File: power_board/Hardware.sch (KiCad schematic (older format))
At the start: 87 parts, among them J1 Conn_01x02, J10 Conn_01x04, J11 Conn_01x04, J12 Conn_02x13_Odd_Even, J13 Conn_01x02, J14 Conn_01x02, J2 Conn_01x04, J3 Conn_01x02, J4 Conn_01x02_Male, J5 Conn_01x02_Male, J6 Conn_01x02_Male, J7 Conn_01x02_Male, J8 Conn_01x03, J9 Conn_01x03, Q1 BD140, Q10 BC548, Q11 BD139, Q12 BD139, Q2 BD140, Q3 BC548, Q4 BC548, Q5 BD139, Q6 BD139, Q7 BD140, Q8 BD140, Q9 BC548, U1 LM393, U2 TCRT5000, U3 LM324, U4 HC-05, U5 TCRT5000

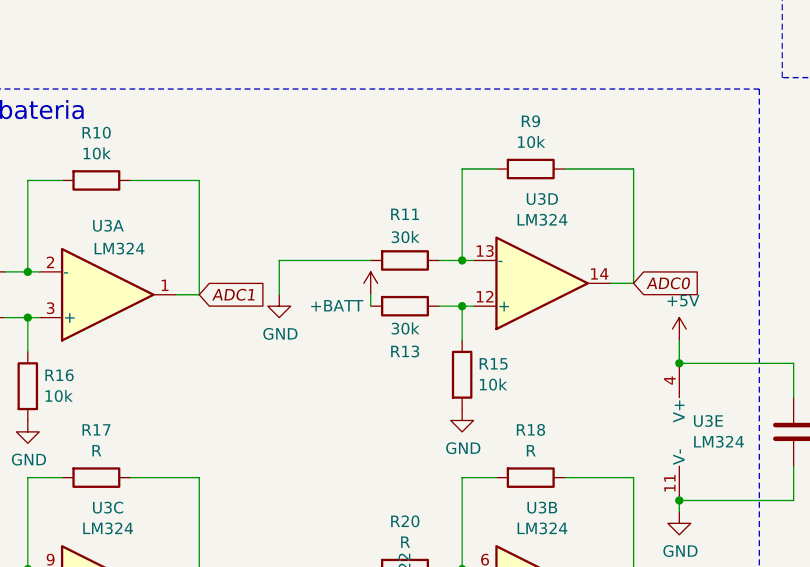
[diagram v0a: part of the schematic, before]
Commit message: Implemented battery class
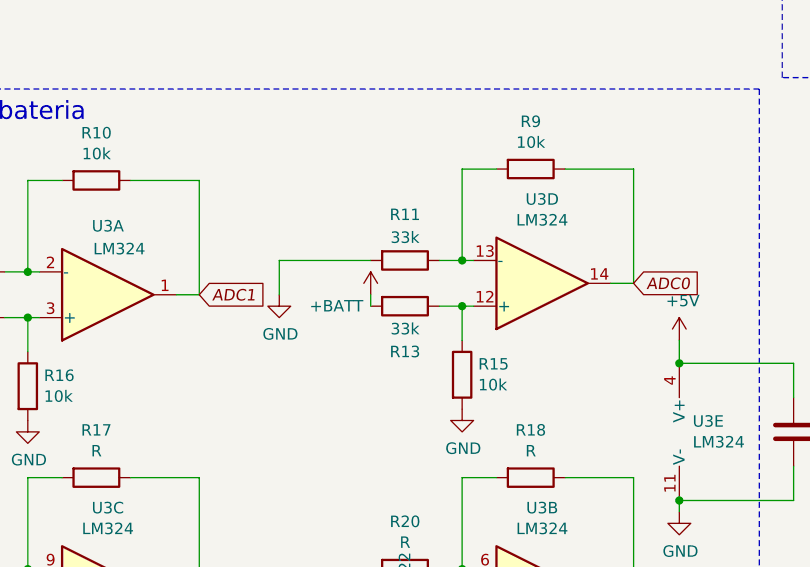
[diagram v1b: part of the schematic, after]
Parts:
- R11, R13: value 30k -> 33k
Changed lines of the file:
@@
 EESchema Schematic File Version 4
-LIBS:Hardware-cache
-EELAYER 26 0
+EELAYER 30 0
 EELAYER END
 $Descr A4 11693 8268
@@
 P 3200 5450
 F 0 "R13" V 3400 5450 50  0000 C CNN
-F 1 "30k" V 3300 5450 50  0000 C CNN
+F 1 "33k" V 3300 5450 50  0000 C CNN
 F 2 "Resistor_SMD:R_0805_2012Metric" V 3130 5450 50  0001 C CNN
 F 3 "~" H 3200 5450 50  0001 C CNN
@@
 P 3200 5250
 F 0 "R11" V 3000 5250 50  0000 C CNN
-F 1 "30k" V 3100 5250 50  0000 C CNN
+F 1 "33k" V 3100 5250 50  0000 C CNN
 F 2 "Resistor_SMD:R_0805_2012Metric" V 3130 5250 50  0001 C CNN
 F 3 "~" H 3200 5250 50  0001 C CNN
